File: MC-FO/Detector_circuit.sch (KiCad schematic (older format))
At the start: 8 parts, among them U141 IFD97, U142 74LVC1G02SE-7

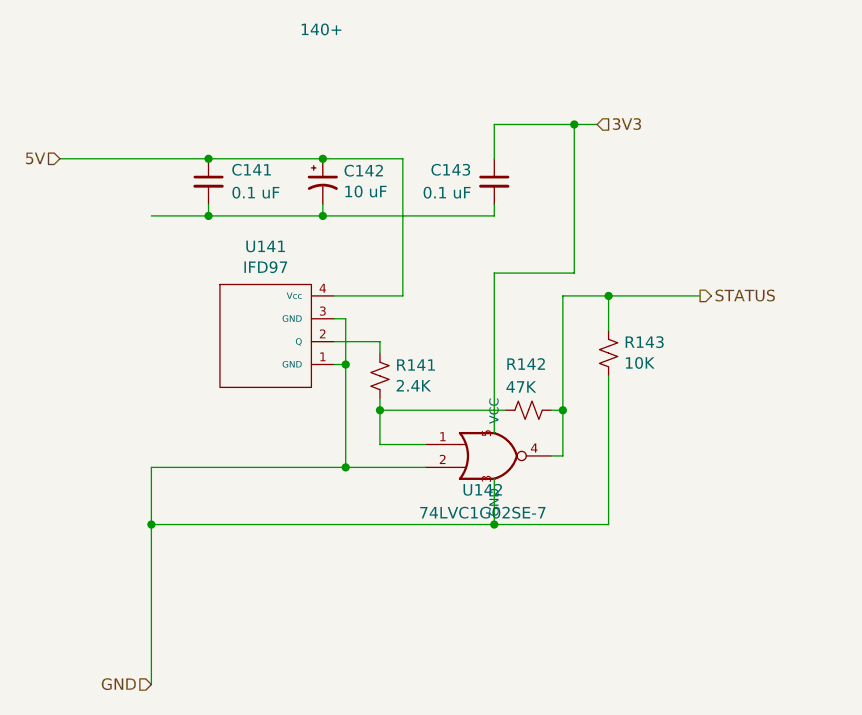
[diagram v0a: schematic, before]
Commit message: updating SAFE_STATE_FLAG and EMITTER_ENABLE
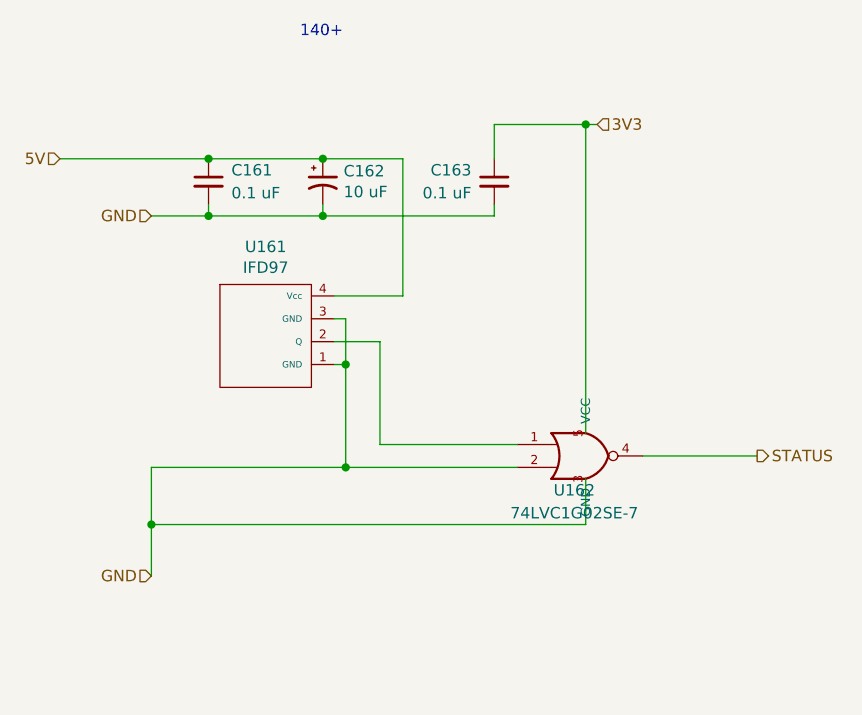
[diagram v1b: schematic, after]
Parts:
- removed R141: 2.4K, Resistor_SMD:R_0603_1608Metric, symbol Device:R_Small_US
- removed R142: 47K, Resistor_SMD:R_0603_1608Metric, symbol Device:R_Small_US
- removed R143: 10K, Resistor_SMD:R_0603_1608Metric, symbol Device:R_Small_US
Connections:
- wire segments 42 -> 29
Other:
- moved on the sheet: U162
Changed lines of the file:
@@
 Wire Wire Line
 	4400 4250 4400 4500
-Wire Wire Line
-	6800 3500 6400 3500
 $Comp
 L Existing_IC_Models:IFD97 U141
@@
 AR Path="/621F57A1/62204747" Ref="U141"  Part="1"
 AR Path="/622415A4/62204747" Ref="U161"  Part="1"
-F 0 "U141" H 4900 4915 50  0000 C CNN
+F 0 "U161" H 4900 4915 50  0000 C CNN
 F 1 "IFD97" H 4900 4824 50  0000 C CNN
 F 2 "Footprints_MC-FO:IFD97" H 4900 4900 50  0001 C CNN
@@
 AR Path="/621F57A1/6220474D" Ref="C141"  Part="1"
 AR Path="/622415A4/6220474D" Ref="C161"  Part="1"
-F 0 "C141" H 4750 3050 50  0000 L CNN
+F 0 "C161" H 4750 3050 50  0000 L CNN
 F 1 "0.1 uF" H 4750 2950 50  0000 L CNN
 F 2 "Capacitor_SMD:C_0603_1608Metric" H 4650 3000 50  0001 C CNN
@@
 AR Path="/621F57A1/62204753" Ref="C142"  Part="1"
 AR Path="/622415A4/62204753" Ref="C162"  Part="1"
-F 0 "C142" H 5241 3046 50  0000 L CNN
+F 0 "C162" H 5241 3046 50  0000 L CNN
 F 1 "10 uF" H 5241 2955 50  0000 L CNN
 F 2 "Capacitor_SMD:C_0603_1608Metric" H 5150 3000 50  0001 C CNN
@@
 Wire Wire Line
 	5150 3150 5150 3100
-$Comp
-L Device:R_Small_US R141
-U 1 1 6220475B
-P 5400 3850
-AR Path="/621F57A1/6220475B" Ref="R141"  Part="1"
-AR Path="/622415A4/6220475B" Ref="R161"  Part="1"
-F 0 "R141" H 5468 3896 50  0000 L CNN
-F 1 "2.4K" H 5468 3805 50  0000 L CNN
-F 2 "Resistor_SMD:R_0603_1608Metric" H 5400 3850 50  0001 C CNN
-F 3 "~" H 5400 3850 50  0001 C CNN
-	1    5400 3850
-	1    0    0    -1
-$EndComp
 Wire Wire Line
-	5400 4150 5600 4150
+	5400 4150 6000 4150
 Connection ~ 5150 2900
 Wire Wire Line
@@
 Wire Wire Line
 	5500 2900 5500 3500
-Wire Wire Line
-	6200 4200 6150 4200
-$Comp
-L Device:R_Small_US R142
-U 1 1 62204767
-P 6050 4000
-AR Path="/621F57A1/62204767" Ref="R142"  Part="1"
-AR Path="/622415A4/62204767" Ref="R162"  Part="1"
-F 0 "R142" V 5850 3900 50  0000 L CNN
-F 1 "47K" V 5950 3900 50  0000 L CNN
-F 2 "Resistor_SMD:R_0603_1608Metric" H 6050 4000 50  0001 C CNN
-F 3 "~" H 6050 4000 50  0001 C CNN
-	1    6050 4000
-	0    1    1    0
-$EndComp
-Wire Wire Line
-	5950 4000 5400 4000
 Wire Wire Line
 	4650 3150 4400 3150
@@
 Connection ~ 5250 4250
 Wire Wire Line
-	5250 4250 5600 4250
-Wire Wire Line
-	5400 3750 5400 3700
+	5250 4250 6000 4250
 Wire Wire Line
 	5400 3700 5200 3700
 Wire Wire Line
-	5400 3950 5400 4000
-Connection ~ 5400 4000
-Wire Wire Line
-	5400 4000 5400 4150
-Wire Wire Line
-	6200 3500 6200 4000
-Wire Wire Line
-	6150 4000 6200 4000
-Connection ~ 6200 4000
-Wire Wire Line
-	6200 4000 6200 4200
-Wire Wire Line
 	4650 2900 4000 2900
 Connection ~ 4650 2900
-$Comp
-L Device:R_Small_US R143
-U 1 1 62204783
-P 6400 3750
-AR Path="/621F57A1/62204783" Ref="R143"  Part="1"
-AR Path="/622415A4/62204783" Ref="R163"  Part="1"
-F 0 "R143" H 6468 3796 50  0000 L CNN
-F 1 "10K" H 6468 3705 50  0000 L CNN
-F 2 "Resistor_SMD:R_0603_1608Metric" H 6400 3750 50  0001 C CNN
-F 3 "~" H 6400 3750 50  0001 C CNN
-	1    6400 3750
-	1    0    0    -1
-$EndComp
 Wire Wire Line
-	5900 3400 5900 4100
+	4400 4500 6300 4500
 Wire Wire Line
-	6200 3500 6400 3500
-Wire Wire Line
-	6400 3850 6400 4500
-Wire Wire Line
-	4400 4500 5900 4500
-Wire Wire Line
-	6400 3650 6400 3500
-Wire Wire Line
-	5900 4300 5900 4500
-Connection ~ 5900 4500
-Wire Wire Line
-	5900 4500 6400 4500
+	6300 4300 6300 4500
 $Comp
 L Device:C_Small C?
@@
 AR Path="/621F57A1/62204798" Ref="C143"  Part="1"
 AR Path="/622415A4/62204798" Ref="C163"  Part="1"
-F 0 "C143" H 6000 3050 50  0000 L CNN
+F 0 "C163" H 6000 3050 50  0000 L CNN
 F 1 "0.1 uF" H 6000 2950 50  0000 L CNN
 F 2 "Capacitor_SMD:C_0603_1608Metric" H 5900 3000 50  0001 C CNN
@@
 Connection ~ 4400 4500
 Wire Wire Line
-	4400 4500 4400 5200
+	4400 4500 4400 4725
 Wire Wire Line
 	4400 4250 5250 4250
-Connection ~ 6400 3500
 $Comp
 L MC-FO:74LVC1G02SE-7 U142
 U 1 1 622047A6
-P 5850 4450
+P 6250 4450
 AR Path="/621F57A1/622047A6" Ref="U142"  Part="1"
 AR Path="/622415A4/622047A6" Ref="U162"  Part="1"
-F 0 "U142" H 5850 4550 50  0000 C CNN
-F 1 "74LVC1G02SE-7" H 5850 4450 50  0000 C CNN
-F 2 "Package_TO_SOT_SMD:SOT-353_SC-70-5" H 5850 4450 50  0001 C CNN
-F 3 "" H 5850 4450 50  0001 C CNN
-	1    5850 4450
+F 0 "U162" H 6250 4550 50  0000 C CNN
+F 1 "74LVC1G02SE-7" H 6250 4450 50  0000 C CNN
+F 2 "Package_TO_SOT_SMD:SOT-353_SC-70-5" H 6250 4450 50  0001 C CNN
+F 3 "" H 6250 4450 50  0001 C CNN
+	1    6250 4450
 	1    0    0    -1
 $EndComp
 Wire Wire Line
-	5900 3400 6250 3400
-Wire Wire Line
-	6250 2750 5900 2750
-Wire Wire Line
 	5900 2750 5900 2900
-Wire Wire Line
-	6250 2750 6250 3400
-Wire Wire Line
-	6250 2750 6350 2750
-Connection ~ 6250 2750
 Text HLabel 6350 2750 2    50   Input ~ 0
 3V3
-Text HLabel 6800 3500 2    50   Output ~ 0
+Text HLabel 7050 4200 2    50   Output ~ 0
 STATUS
 Text HLabel 4000 2900 0    50   Input ~ 0
 5V
-Text HLabel 4400 5200 0    50   Input ~ 0
+Text HLabel 4400 4725 0    50   Input ~ 0
 GND
 Text Notes 5050 2375 0    50   ~ 0
 140+
+Text HLabel 4400 3150 0    50   Input ~ 0
+GND
+Wire Wire Line
+	5400 3700 5400 4150
+Wire Wire Line
+	6550 4200 7050 4200
+Wire Wire Line
+	5900 2750 6300 2750
+Connection ~ 6300 2750
+Wire Wire Line
+	6300 2750 6350 2750
+Wire Wire Line
+	6300 2750 6300 4100
 $EndSCHEMATC

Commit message: schematic changes--> layout rev
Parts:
- added TP141: TestPoint, TestPoint:TestPoint_Pad_D2.0mm, symbol Connector:TestPoint
- U142: footprint Package_TO_SOT_SMD:SOT-353_SC-70-5 -> Package_TO_SOT_SMD:SOT-353_SC-70-5_Handsoldering
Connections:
- net STATUS: now also TP141.1
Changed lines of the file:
@@
 AR Path="/621F57A1/622047A6" Ref="U142"  Part="1"
 AR Path="/622415A4/622047A6" Ref="U162"  Part="1"
+AR Path="/6175812E/622047A6" Ref="U162"  Part="1"
 F 0 "U162" H 6250 4550 50  0000 C CNN
 F 1 "74LVC1G02SE-7" H 6250 4450 50  0000 C CNN
-F 2 "Package_TO_SOT_SMD:SOT-353_SC-70-5" H 6250 4450 50  0001 C CNN
-F 3 "" H 6250 4450 50  0001 C CNN
+F 2 "Package_TO_SOT_SMD:SOT-353_SC-70-5_Handsoldering" H 6250 4450 50  0001 C CNN
+F 3 "https://www.diodes.com/assets/Datasheets/74LVC1G02.pdf" H 6250 4450 50  0001 C CNN
 	1    6250 4450
 	1    0    0    -1
@@
 	5400 3700 5400 4150
 Wire Wire Line
-	6550 4200 7050 4200
+	6550 4200 6775 4200
+$Comp
+L Connector:TestPoint TP?
+U 1 1 623CF240
+P 6775 4200
+AR Path="/623CF240" Ref="TP?"  Part="1"
+AR Path="/621F57A1/623CF240" Ref="TP141"  Part="1"
+AR Path="/622415A4/623CF240" Ref="TP161"  Part="1"
+F 0 "TP161" H 6833 4318 50  0000 L CNN
+F 1 "TestPoint" H 6825 4425 50  0000 L CNN
+F 2 "TestPoint:TestPoint_Pad_D2.0mm" H 6975 4200 50  0001 C CNN
+F 3 "~" H 6975 4200 50  0001 C CNN
+	1    6775 4200
+	1    0    0    1
+$EndComp
+Connection ~ 6775 4200
 Wire Wire Line
-	5900 2750 6300 2750
+	6775 4200 7050 4200
 Connection ~ 6300 2750
 Wire Wire Line
 	6300 2750 6350 2750
 Wire Wire Line
+	5900 2750 6300 2750
+Wire Wire Line
 	6300 2750 6300 4100

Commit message: Add files via upload
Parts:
- U142: symbol MC-FO:74LVC1G02SE-7 -> Existing_IC_Models:74LVC1G02SE-7
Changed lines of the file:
@@
 	4400 4250 5250 4250
 $Comp
-L MC-FO:74LVC1G02SE-7 U142
+L Existing_IC_Models:74LVC1G02SE-7 U142
 U 1 1 622047A6
 P 6250 4450

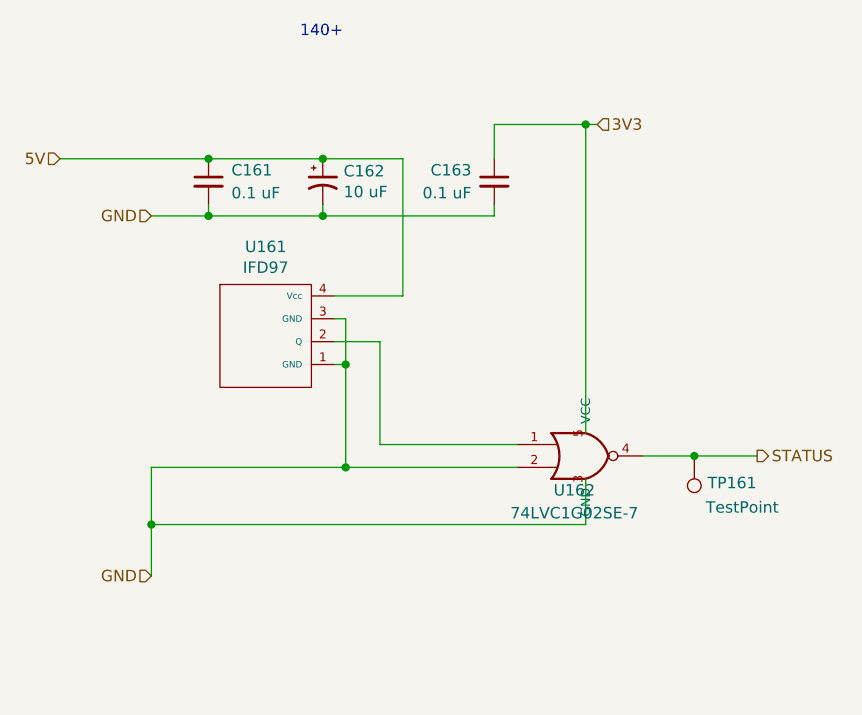
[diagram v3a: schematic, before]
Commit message: Layout Revision
-removed MH1 from emitter/detector symbol
-pin out changes to assist with routing on the backplane
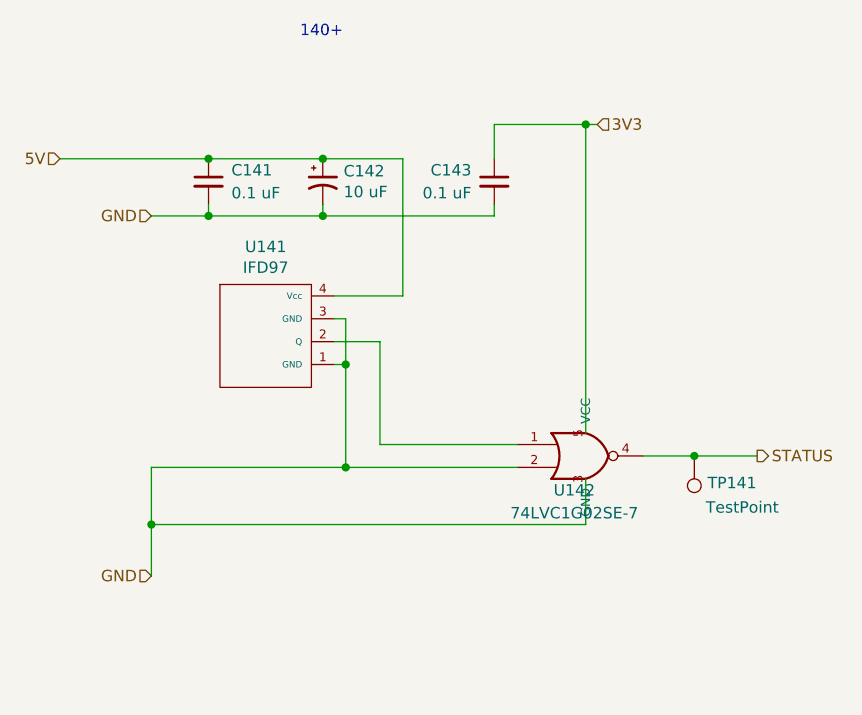
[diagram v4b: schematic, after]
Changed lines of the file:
@@
 $Descr A4 11693 8268
 encoding utf-8
-Sheet 10 11
+Sheet 11 11
 Title ""
 Date ""
@@
 AR Path="/621F57A1/62204747" Ref="U141"  Part="1"
 AR Path="/622415A4/62204747" Ref="U161"  Part="1"
-F 0 "U161" H 4900 4915 50  0000 C CNN
+F 0 "U141" H 4900 4915 50  0000 C CNN
 F 1 "IFD97" H 4900 4824 50  0000 C CNN
 F 2 "Footprints_MC-FO:IFD97" H 4900 4900 50  0001 C CNN
@@
 AR Path="/621F57A1/6220474D" Ref="C141"  Part="1"
 AR Path="/622415A4/6220474D" Ref="C161"  Part="1"
-F 0 "C161" H 4750 3050 50  0000 L CNN
+F 0 "C141" H 4750 3050 50  0000 L CNN
 F 1 "0.1 uF" H 4750 2950 50  0000 L CNN
 F 2 "Capacitor_SMD:C_0603_1608Metric" H 4650 3000 50  0001 C CNN
@@
 AR Path="/621F57A1/62204753" Ref="C142"  Part="1"
 AR Path="/622415A4/62204753" Ref="C162"  Part="1"
-F 0 "C162" H 5241 3046 50  0000 L CNN
+F 0 "C142" H 5241 3046 50  0000 L CNN
 F 1 "10 uF" H 5241 2955 50  0000 L CNN
 F 2 "Capacitor_SMD:C_0603_1608Metric" H 5150 3000 50  0001 C CNN
@@
 AR Path="/621F57A1/62204798" Ref="C143"  Part="1"
 AR Path="/622415A4/62204798" Ref="C163"  Part="1"
-F 0 "C163" H 6000 3050 50  0000 L CNN
+F 0 "C143" H 6000 3050 50  0000 L CNN
 F 1 "0.1 uF" H 6000 2950 50  0000 L CNN
 F 2 "Capacitor_SMD:C_0603_1608Metric" H 5900 3000 50  0001 C CNN
@@
 AR Path="/622415A4/622047A6" Ref="U162"  Part="1"
 AR Path="/6175812E/622047A6" Ref="U162"  Part="1"
-F 0 "U162" H 6250 4550 50  0000 C CNN
+F 0 "U142" H 6250 4550 50  0000 C CNN
 F 1 "74LVC1G02SE-7" H 6250 4450 50  0000 C CNN
 F 2 "Package_TO_SOT_SMD:SOT-353_SC-70-5_Handsoldering" H 6250 4450 50  0001 C CNN
@@
 AR Path="/621F57A1/623CF240" Ref="TP141"  Part="1"
 AR Path="/622415A4/623CF240" Ref="TP161"  Part="1"
-F 0 "TP161" H 6833 4318 50  0000 L CNN
+F 0 "TP141" H 6833 4318 50  0000 L CNN
 F 1 "TestPoint" H 6825 4425 50  0000 L CNN
 F 2 "TestPoint:TestPoint_Pad_D2.0mm" H 6975 4200 50  0001 C CNN
